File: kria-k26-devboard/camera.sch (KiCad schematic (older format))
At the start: 23 parts, among them J3 WE_68715014522, U10 PI4MSD5V9540BUEX, U11 AP7340-18FS4-7

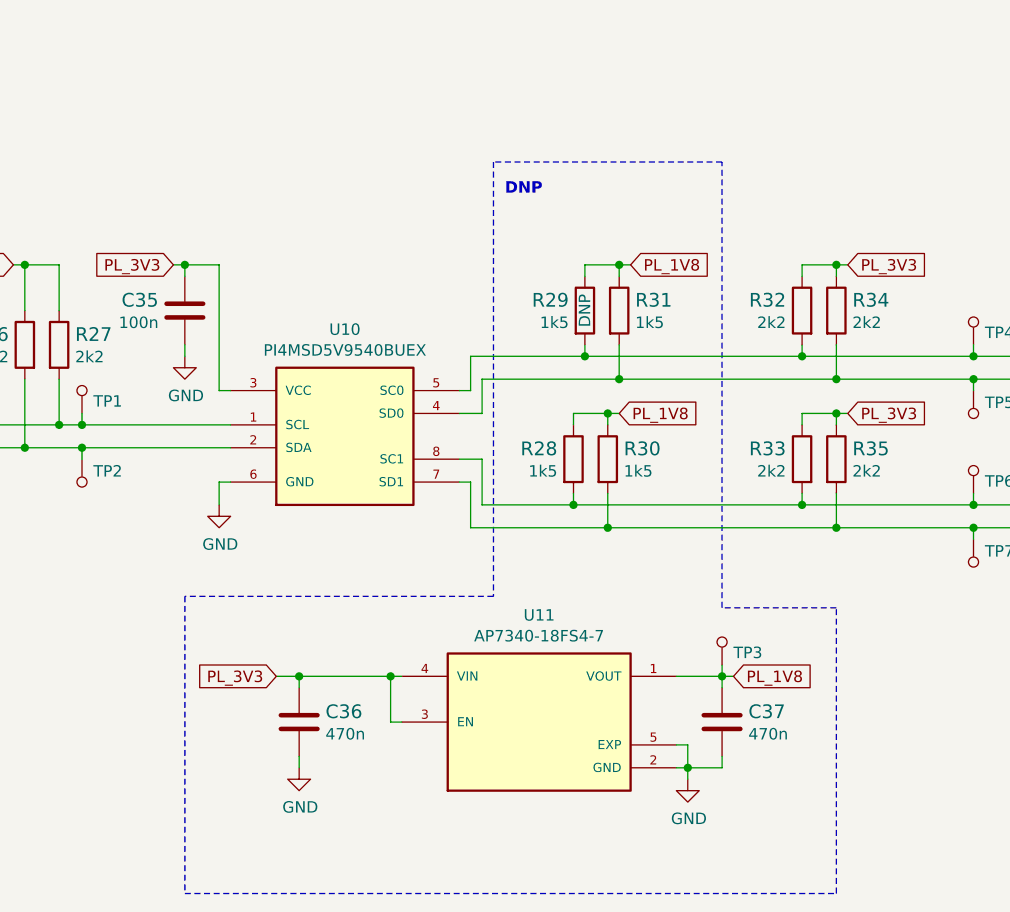
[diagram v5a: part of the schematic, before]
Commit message: Finished implementing changes after the review, fixed ETH led connections, length matching fixed and double checked with external script
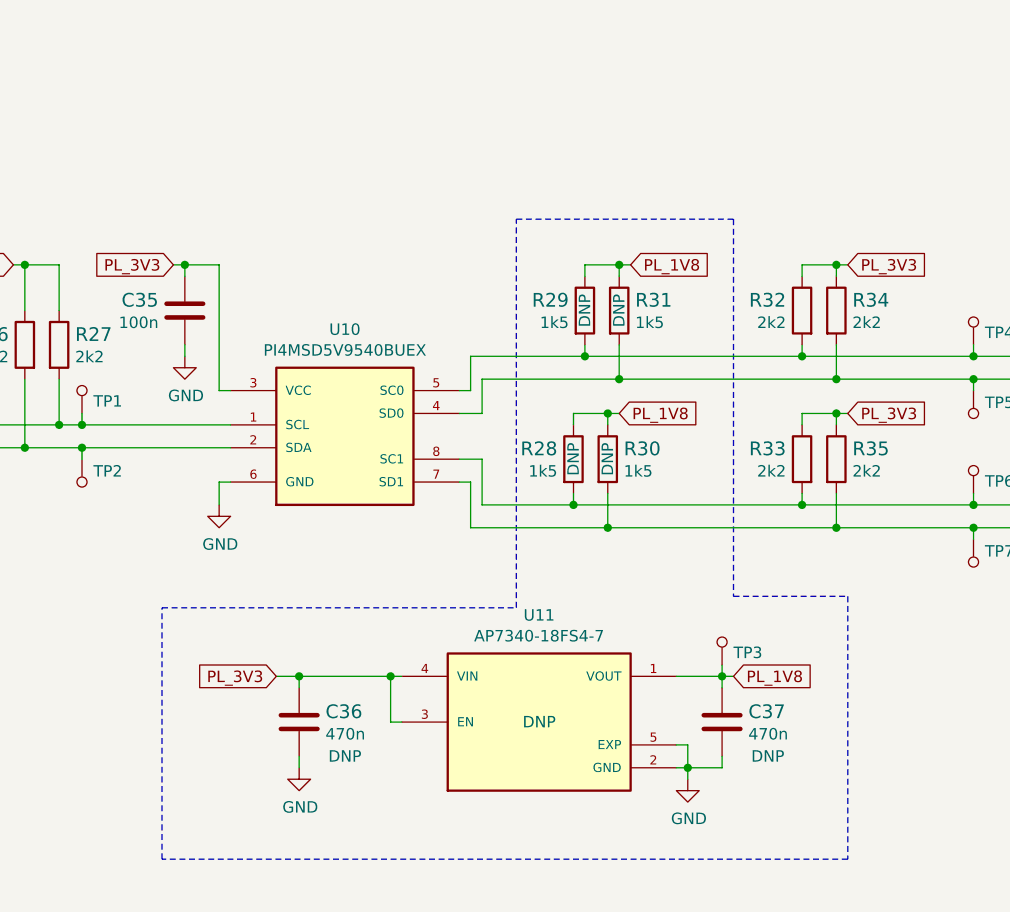
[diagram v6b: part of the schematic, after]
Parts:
- C36, C37, R28, R30, R31, U11: DNP (none) -> DNP
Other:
- note removed: "DNP"
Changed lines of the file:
@@
 encoding utf-8
 Sheet 5 19
-Title ""
+Title "Camera interface"
 Date "2022-03-10"
 Rev "1.0.0"
@@
 F 5 "MP000515" H 4150 4600 60  0001 L CNN "MPN"
 F 6 "1k5" V 4003 4370 50  0000 L CNN "Val"
+F 7 "DNP" H 3950 4300 50  0000 C CNN "DNP"
 	1    3950 4300
 	0    1    1    0
@@
 F 5 "MP000515" H 4100 5250 60  0001 L CNN "MPN"
 F 6 "1k5" V 3953 5020 50  0000 L CNN "Val"
+F 7 "DNP" H 3900 4950 50  0000 C CNN "DNP"
 	1    3900 4950
 	0    1    1    0
@@
 F 5 "MP000515" H 3950 5250 60  0001 L CNN "MPN"
 F 6 "1k5" V 3803 4880 50  0000 R CNN "Val"
+F 7 "DNP" H 3750 4950 50  0000 C CNN "DNP"
 	1    3750 4950
 	0    1    1    0
@@
 Text GLabel 3950 4750 2    50   Input ~ 0
 PL_1V8
-Text Notes 3450 3800 0    50   ~ 10
-DNP
 $Comp
 L antmicroPMICVoltageRegulatorsLinear:AP7340-18FS4-7 U11
@@
 F 4 "AP7340-18FS4-7" H 3500 5550 50  0001 C CNN "MPN"
 F 5 "Diodes Incorporated" H 3550 5650 50  0001 C CNN "Manufacturer"
+F 6 "DNP" H 3600 6100 50  0000 C CNN "DNP"
 	1    3600 6100
 	1    0    0    -1
@@
 F 5 "C1005X5R1E474M050BB" H 2750 6400 60  0001 L CNN "MPN"
 F 6 "470n" H 2665 6047 50  0000 L CNN "Val"
+F 7 "DNP" H 2750 5950 50  0000 C CNN "DNP"
 	1    2550 6100
 	1    0    0    -1
@@
 F 5 "C1005X5R1E474M050BB" H 4600 6400 60  0001 L CNN "MPN"
 F 6 "470n" H 4515 6047 50  0000 L CNN "Val"
+F 7 "DNP" H 4600 5950 50  0000 C CNN "DNP"
 	1    4400 6100
 	1    0    0    -1
@@
 Wire Wire Line
 	4900 5250 5500 5250
-Wire Notes Line
-	3400 5550 2050 5550
-Wire Notes Line
-	2050 5550 2050 6850
-Wire Notes Line
-	2050 6850 4900 6850
-Wire Notes Line
-	4900 6850 4900 5600
-Wire Notes Line
-	4900 5600 4400 5600
-Wire Notes Line
-	4400 5600 4400 3650
-Wire Notes Line
-	4400 3650 3400 3650
-Wire Notes Line
-	3400 3650 3400 5550
 Wire Wire Line
 	4200 6300 4250 6300
@@
 Wire Wire Line
 	5500 4500 5700 4500
+Wire Notes Line
+	3500 3900 4450 3900
+Wire Notes Line
+	4450 3900 4450 5550
+Wire Notes Line
+	4450 5550 4950 5550
+Wire Notes Line
+	4950 5550 4950 6700
+Wire Notes Line
+	4950 6700 1950 6700
+Wire Notes Line
+	1950 6700 1950 5600
+Wire Notes Line
+	1950 5600 3500 5600
+Wire Notes Line
+	3500 5600 3500 3900
 $EndSCHEMATC

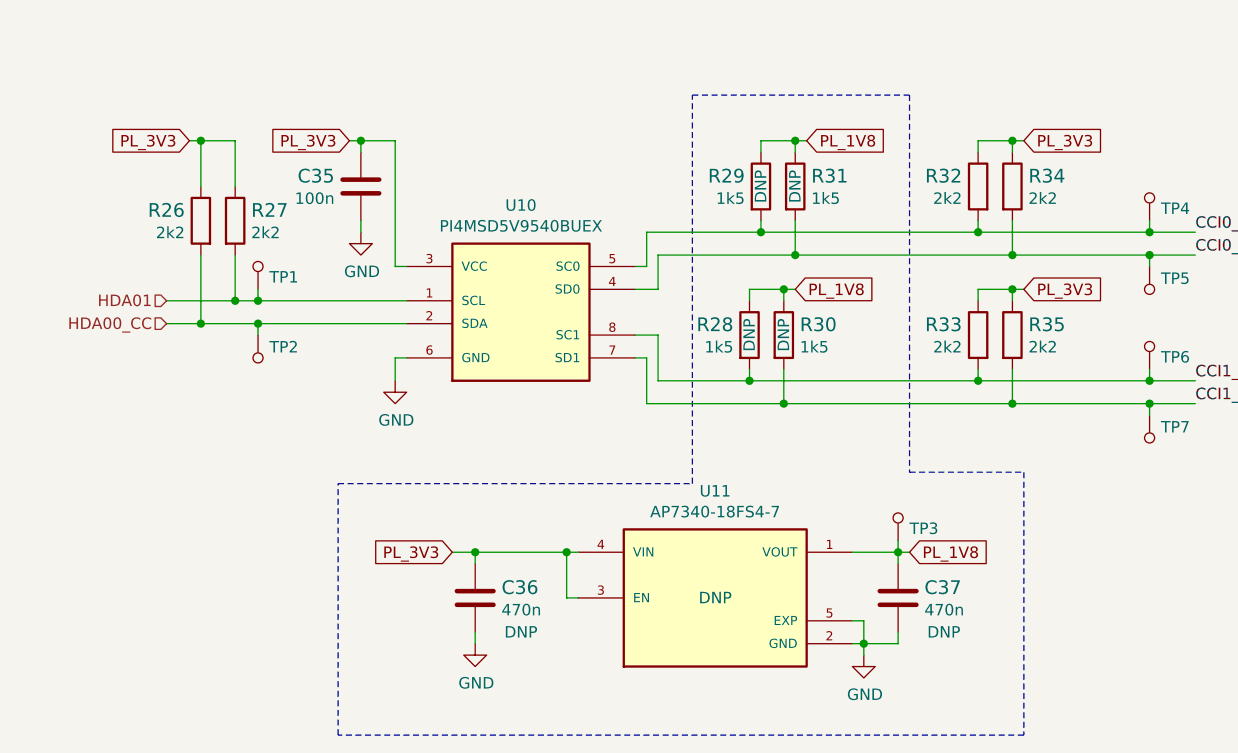
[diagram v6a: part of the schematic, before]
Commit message: Replaced 4A DC-DC conventer, finished cleaning after replacement
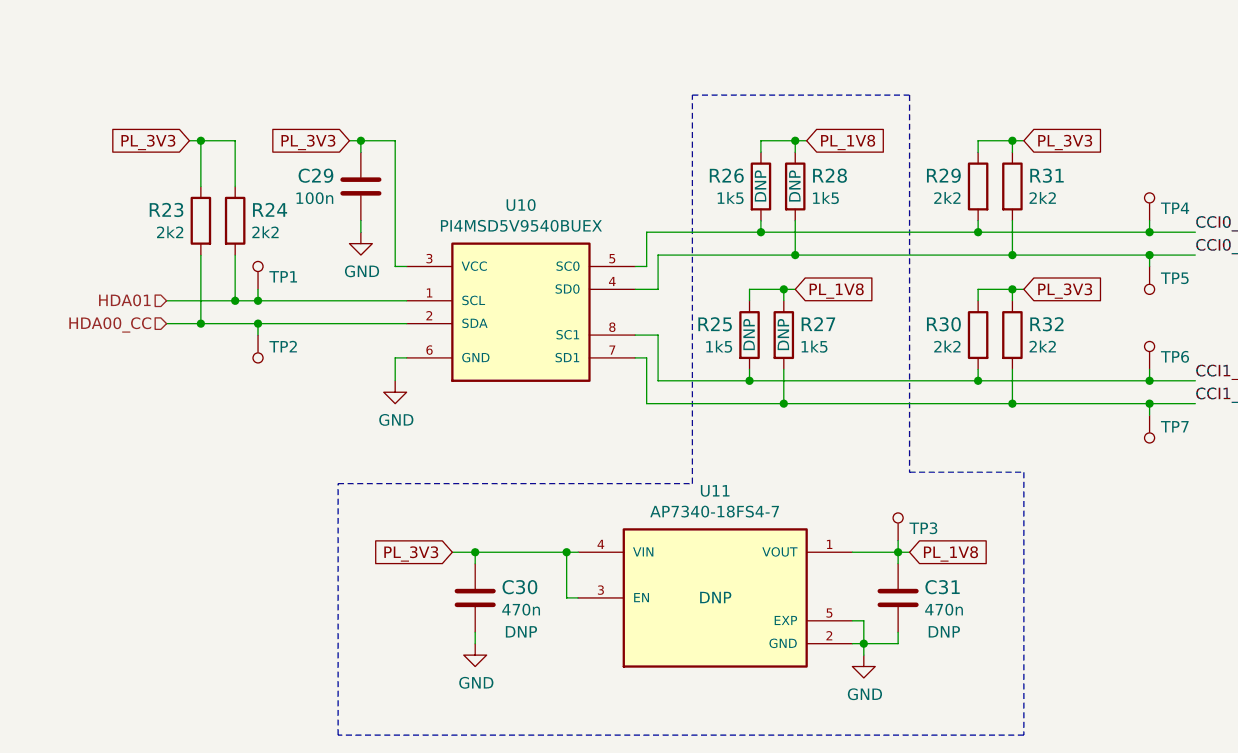
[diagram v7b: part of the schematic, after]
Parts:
- renumbered C35 to C29, C36 to C30, C37 to C31, R26 to R23, R27 to R24, R28 to R25, R29 to R26, R30 to R27, R31 to R28, R32 to R29, R33 to R30, R34 to R31, R35 to R32
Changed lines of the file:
@@
 	2050 4100 2200 4100
 $Comp
-L power:GND #PWR056
+L power:GND #PWR051
 U 1 1 64C03362
 P 2050 4500
-F 0 "#PWR056" H 2050 4250 50  0001 C CNN
+F 0 "#PWR051" H 2050 4250 50  0001 C CNN
 F 1 "GND" H 2055 4327 50  0000 C CNN
 F 2 "" H 2050 4500 50  0001 C CNN
@@
 	2200 4650 2250 4650
 $Comp
-L power:GND #PWR057
+L power:GND #PWR052
 U 1 1 64C26FC9
 P 2200 5150
-F 0 "#PWR057" H 2200 4900 50  0001 C CNN
+F 0 "#PWR052" H 2200 4900 50  0001 C CNN
 F 1 "GND" H 2205 4977 50  0000 C CNN
 F 2 "" H 2200 5150 50  0001 C CNN
@@
 	4750 5100 4750 5150
 $Comp
-L antmicroResistors0402:R_2k2_0402 R35
+L antmicroResistors0402:R_2k2_0402 R32
 U 1 1 649B3ABE
 P 4900 4950
-F 0 "R35" V 4855 5020 60  0000 L CNN
+F 0 "R32" V 4855 5020 60  0000 L CNN
 F 1 "R_2k2_0402" H 4900 4800 60  0001 C CNN
 F 2 "antmicro-footprints:0402-res" H 5100 5150 60  0001 L CNN
@@
 $EndComp
 $Comp
-L antmicroResistors0402:R_2k2_0402 R33
+L antmicroResistors0402:R_2k2_0402 R30
 U 1 1 649A89C1
 P 4750 4950
-F 0 "R33" V 4705 5020 60  0000 L CNN
+F 0 "R30" V 4705 5020 60  0000 L CNN
 F 1 "R_2k2_0402" H 4750 4800 60  0001 C CNN
 F 2 "antmicro-footprints:0402-res" H 4950 5150 60  0001 L CNN
@@
 	4750 4450 4750 4500
 $Comp
-L antmicroResistors0402:R_2k2_0402 R34
+L antmicroResistors0402:R_2k2_0402 R31
 U 1 1 64B09B58
 P 4900 4300
-F 0 "R34" V 4855 4370 60  0000 L CNN
+F 0 "R31" V 4855 4370 60  0000 L CNN
 F 1 "R_2k2_0402" H 4900 4150 60  0001 C CNN
 F 2 "antmicro-footprints:0402-res" H 5100 4500 60  0001 L CNN
@@
 $EndComp
 $Comp
-L antmicroResistors0402:R_2k2_0402 R32
+L antmicroResistors0402:R_2k2_0402 R29
 U 1 1 64B09B4B
 P 4750 4300
-F 0 "R32" V 4705 4370 60  0000 L CNN
+F 0 "R29" V 4705 4370 60  0000 L CNN
 F 1 "R_2k2_0402" H 4750 4150 60  0001 C CNN
 F 2 "antmicro-footprints:0402-res" H 4950 4500 60  0001 L CNN
@@
 PL_3V3
 $Comp
-L antmicroResistors0402:R_2k2_0402 R27
+L antmicroResistors0402:R_2k2_0402 R24
 U 1 1 64DE55BF
 P 1500 4450
-F 0 "R27" V 1455 4520 60  0000 L CNN
+F 0 "R24" V 1455 4520 60  0000 L CNN
 F 1 "R_2k2_0402" H 1500 4300 60  0001 C CNN
 F 2 "antmicro-footprints:0402-res" H 1700 4650 60  0001 L CNN
@@
 $EndComp
 $Comp
-L antmicroResistors0402:R_2k2_0402 R26
+L antmicroResistors0402:R_2k2_0402 R23
 U 1 1 64DE573E
 P 1350 4450
-F 0 "R26" V 1305 4520 60  0000 L CNN
+F 0 "R23" V 1305 4520 60  0000 L CNN
 F 1 "R_2k2_0402" H 1350 4300 60  0001 C CNN
 F 2 "antmicro-footprints:0402-res" H 1550 4650 60  0001 L CNN
@@
 PL_3V3
 $Comp
-L antmicroCapacitors0402:C_100n_0402 C35
+L antmicroCapacitors0402:C_100n_0402 C29
 U 1 1 65AE161E
 P 2050 4300
-F 0 "C35" H 2165 4345 60  0000 L CNN
+F 0 "C29" H 2165 4345 60  0000 L CNN
 F 1 "C_100n_0402" H 2050 4150 60  0001 C CNN
 F 2 "antmicro-footprints:0402-cap" H 2250 4500 60  0001 L CNN
@@
 Camera interface
 $Comp
-L power:GND #PWR060
+L power:GND #PWR055
 U 1 1 6733CCE5
 P 8350 5800
-F 0 "#PWR060" H 8350 5550 50  0001 C CNN
+F 0 "#PWR055" H 8350 5550 50  0001 C CNN
 F 1 "GND" H 8355 5627 50  0000 C CNN
 F 2 "" H 8350 5800 50  0001 C CNN
@@
 	3900 5250 4900 5250
 $Comp
-L antmicroResistors0402:R_1k5_0402 R31
+L antmicroResistors0402:R_1k5_0402 R28
 U 1 1 62884B6D
 P 3950 4300
-F 0 "R31" V 3905 4370 60  0000 L CNN
+F 0 "R28" V 3905 4370 60  0000 L CNN
 F 1 "R_1k5_0402" H 3950 4150 60  0001 C CNN
 F 2 "antmicro-footprints:0402-res" H 4150 4500 60  0001 L CNN
@@
 $EndComp
 $Comp
-L antmicroResistors0402:R_1k5_0402 R29
+L antmicroResistors0402:R_1k5_0402 R26
 U 1 1 6288E001
 P 3800 4300
-F 0 "R29" V 3755 4230 60  0000 R CNN
+F 0 "R26" V 3755 4230 60  0000 R CNN
 F 1 "R_1k5_0402" H 3800 4150 60  0001 C CNN
 F 2 "antmicro-footprints:0402-res" H 4000 4500 60  0001 L CNN
@@
 $EndComp
 $Comp
-L antmicroResistors0402:R_1k5_0402 R30
+L antmicroResistors0402:R_1k5_0402 R27
 U 1 1 628A1FB5
 P 3900 4950
-F 0 "R30" V 3855 5020 60  0000 L CNN
+F 0 "R27" V 3855 5020 60  0000 L CNN
 F 1 "R_1k5_0402" H 3900 4800 60  0001 C CNN
 F 2 "antmicro-footprints:0402-res" H 4100 5150 60  0001 L CNN
@@
 $EndComp
 $Comp
-L antmicroResistors0402:R_1k5_0402 R28
+L antmicroResistors0402:R_1k5_0402 R25
 U 1 1 628A2134
 P 3750 4950
-F 0 "R28" V 3705 4880 60  0000 R CNN
+F 0 "R25" V 3705 4880 60  0000 R CNN
 F 1 "R_1k5_0402" H 3750 4800 60  0001 C CNN
 F 2 "antmicro-footprints:0402-res" H 3950 5150 60  0001 L CNN
@@
 Connection ~ 2950 5900
 $Comp
-L antmicroCapacitors0402:C_470n_0402 C36
+L antmicroCapacitors0402:C_470n_0402 C30
 U 1 1 62A54360
 P 2550 6100
-F 0 "C36" H 2665 6145 60  0000 L CNN
+F 0 "C30" H 2665 6145 60  0000 L CNN
 F 1 "C_470n_0402" H 2550 5950 60  0001 C CNN
 F 2 "antmicro-footprints:0402-cap" H 2750 6300 60  0001 L CNN
@@
 $EndComp
 $Comp
-L antmicroCapacitors0402:C_470n_0402 C37
+L antmicroCapacitors0402:C_470n_0402 C31
 U 1 1 62A6AE5F
 P 4400 6100
-F 0 "C37" H 4515 6145 60  0000 L CNN
+F 0 "C31" H 4515 6145 60  0000 L CNN
 F 1 "C_470n_0402" H 4400 5950 60  0001 C CNN
 F 2 "antmicro-footprints:0402-cap" H 4600 6300 60  0001 L CNN
@@
 	4200 5900 4400 5900
 $Comp
-L power:GND #PWR058
+L power:GND #PWR053
 U 1 1 62A87F4F
 P 2550 6300
-F 0 "#PWR058" H 2550 6050 50  0001 C CNN
+F 0 "#PWR053" H 2550 6050 50  0001 C CNN
 F 1 "GND" H 2555 6127 50  0000 C CNN
 F 2 "" H 2550 6300 50  0001 C CNN
@@
 	4400 6300 4400 6250
 $Comp
-L power:GND #PWR059
+L power:GND #PWR054
 U 1 1 62A973E6
 P 4250 6350
-F 0 "#PWR059" H 4250 6100 50  0001 C CNN
+F 0 "#PWR054" H 4250 6100 50  0001 C CNN
 F 1 "GND" H 4255 6177 50  0000 C CNN
 F 2 "" H 4250 6350 50  0001 C CNN

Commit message: Locklib+ added layer table
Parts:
- C29: footprint antmicro-footprints:0402-cap -> kria-k26-devboard-footprints:0402-cap; symbol antmicroCapacitors0402:C_100n_0402 -> kria-k26-devboard:C_100n_0402
- C30, C31: footprint antmicro-footprints:0402-cap -> kria-k26-devboard-footprints:0402-cap; symbol antmicroCapacitors0402:C_470n_0402 -> kria-k26-devboard:C_470n_0402
- J3: footprint antmicro-footprints:WE_68715014522 -> kria-k26-devboard-footprints:WE_68715014522; symbol antmicroFCCConnectors:WE_68715014522 -> kria-k26-devboard:WE_68715014522
- R23, R24, R29, R30, R31, R32: footprint antmicro-footprints:0402-res -> kria-k26-devboard-footprints:0402-res; symbol antmicroResistors0402:R_2k2_0402 -> kria-k26-devboard:R_2k2_0402
- R25, R26, R27, R28: footprint antmicro-footprints:0402-res -> kria-k26-devboard-footprints:0402-res; symbol antmicroResistors0402:R_1k5_0402 -> kria-k26-devboard:R_1k5_0402
- TP1, TP2, TP3, TP4, TP5, TP6, TP7: footprint antmicro-footprints:Testpoint_smd_0_75mm -> kria-k26-devboard-footprints:Testpoint_smd_0_75mm; symbol antmicroTestPoints:TP_SMD_0_75MM -> kria-k26-devboard:TP_SMD_0_75MM
- U10: footprint antmicro-footprints:MSOP-8_W3mm_PITCH0.65mm -> kria-k26-devboard-footprints:MSOP-8_W3mm_PITCH0.65mm; symbol antmicroLogicSignalSwitchesMultiplexersDecoders:PI4MSD5V9540BUEX -> kria-k26-devboard:PI4MSD5V9540BUEX
- U11: footprint antmicro-footprints:XDFN4 -> kria-k26-devboard-footprints:XDFN4; symbol antmicroPMICVoltageRegulatorsLinear:AP7340-18FS4-7 -> kria-k26-devboard:AP7340-18FS4-7
